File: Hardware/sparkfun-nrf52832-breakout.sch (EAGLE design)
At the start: 48 parts, among them J5 CORTEX_DEBUGPTH, U1 AP2112K-3.3V, U2 NRF52832, Y1 32MHz, Y2 32.768kHz

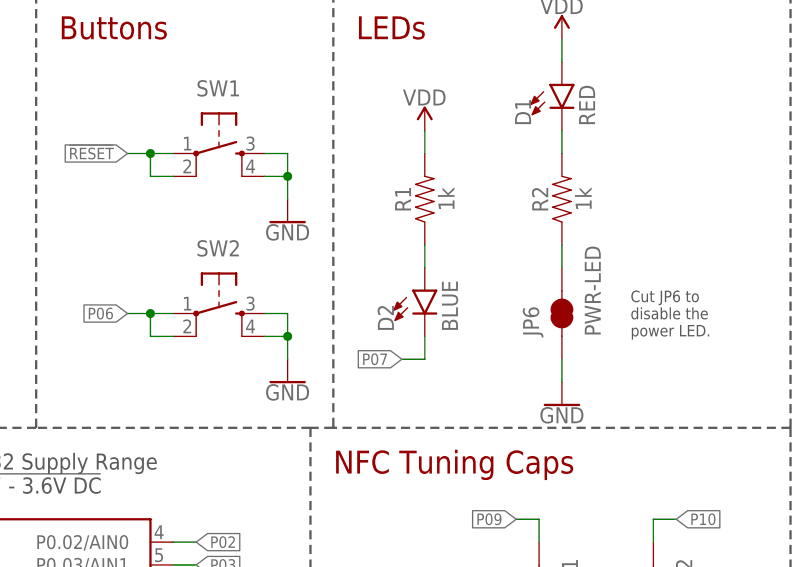
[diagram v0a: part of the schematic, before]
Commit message: Adding of Values to SW1 and SW2
3D Model Modification
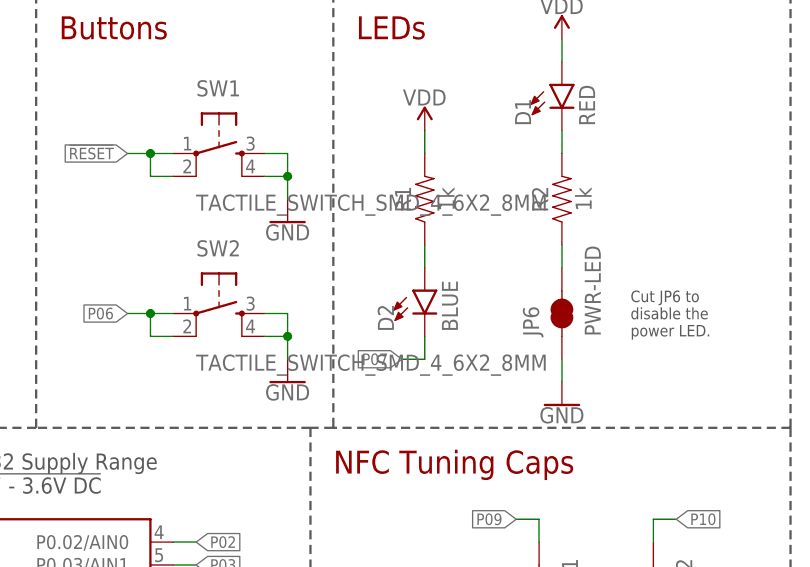
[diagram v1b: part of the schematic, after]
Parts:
- SW1, SW2: value (none) -> TACTILE_SWITCH_SMD_4_6X2_8MM
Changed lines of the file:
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@@
 <?xml version="1.0" encoding="utf-8"?>
 <!DOCTYPE eagle SYSTEM "eagle.dtd">
-<eagle version="7.5.0">
+<eagle version="7.7.0">
 <drawing>
 <settings>
@@
 <part name="SUPPLY1" library="SparkFun-PowerSymbols" deviceset="VIN" device=""/>
 <part name="J5" library="SparkFun-Connectors" deviceset="CORTEX_DEBUG" device="PTH" value="CORTEX_DEBUGPTH"/>
-<part name="SW1" library="SparkFun-Electromechanical" deviceset="SWITCH_SPST_4_PIN" device="RECT"/>
-<part name="SW2" library="SparkFun-Electromechanical" deviceset="SWITCH_SPST_4_PIN" device="RECT"/>
+<part name="SW1" library="SparkFun-Electromechanical" deviceset="SWITCH_SPST_4_PIN" device="RECT" value="TACTILE_SWITCH_SMD_4_6X2_8MM"/>
+<part name="SW2" library="SparkFun-Electromechanical" deviceset="SWITCH_SPST_4_PIN" device="RECT" value="TACTILE_SWITCH_SMD_4_6X2_8MM"/>
 <part name="D1" library="SparkFun-LED" deviceset="LED-RED" device="0603" value="RED"/>
 <part name="D2" library="SparkFun-LED" deviceset="LED-BLUE" device="0603" value="BLUE"/>
